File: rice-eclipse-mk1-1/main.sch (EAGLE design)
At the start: 136 parts, among them IC1 LMV321LICTRT, IC2 LMV321LICTRT, IC3 LMV321LICTRT, IC4 LMV321LICTRT, IC5 UA78M, IC6 LMV321LICTRT, IC7 LMV321LICTRT, IC8 LMV321LICTRT, IC9 LMV321LICTRT, U1 LM1084ISX-5.0/NOPB, U2 THS4531IDRD8-M, U3 THS4531IDRD8-M, U4 THS4531IDRD8-M, U5 THS4531IDRD8-M, U6 1101M2S3CQE2

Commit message: Fixed board files maybe.
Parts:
- removed LED4: (no value), led:LED5MM
- added +10V_LED: (no value), led:LED5MM
- added PWR_DEBUG: (no value), con-phoenix-254:MPT5
- added RPI_DEBUG: (no value), con-phoenix-254:MPT7
- C14, C15, C18, C21, C24, C27, C8, C9: value 10nF -> 0.1UF; device rcl:C-USC0402K -> rcl:C-USC0603
- renumbered IC5 to 10V_REG, LED1 to +12V_LED, LED2 to +5V_LED, LED3 to +3.3V_LED, REG1 to 3.3V_REG, U$1 to PWR_IN, U$4 to PWR_OUT1, U$5 to PWR_OUT2, U$6 to SOL+RELAY, U$7 to SOLENOIDS, U1 to 5V_REG
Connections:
- net +10V: now also PWR_DEBUG-2.1, PWR_OUT1G$1.1; no longer PWR_OUT1G$2.2
- net +12V: now also PWR_DEBUG-1.1, PWR_OUT1G$2.2; no longer PWR_OUT1G$1.1
- net +3V3: now also PWR_DEBUG-4.1, PWR_OUT2G$1.1
- net +5V: now also PWR_DEBUG-3.1, PWR_OUT2G$2.2; no longer PWR_OUT2G$1.1
- net ADC1_CS: now also RPI_DEBUG-4.1
- net ADC2_CS: now also RPI_DEBUG-3.1
- net ADC3_CS: now also RPI_DEBUG-2.1
- net GND: now also +10V_LED.C, PWR_DEBUG-5.1, RPI_DEBUG-1.1; no longer LED4.A, PWR_OUT2G$2.2
- net MISO: now also RPI_DEBUG-6.1
- net MOSI: now also RPI_DEBUG-5.1
- net N$9: now also +10V_LED.A; no longer LED4.C
- net SCLK: now also RPI_DEBUG-7.1

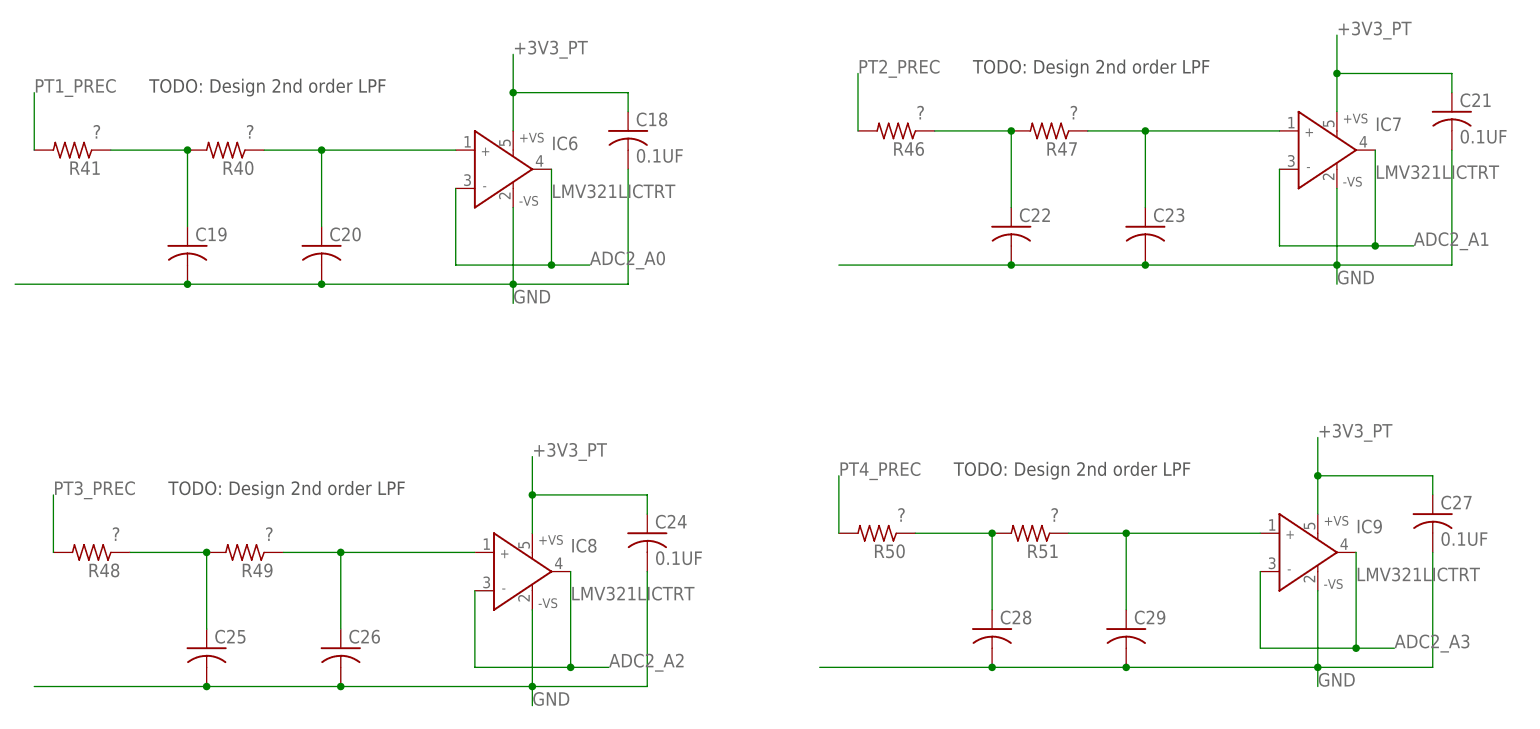
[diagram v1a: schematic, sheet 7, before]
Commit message: Fixed major known bugs in board design.
* 5V power rail for AA voltage follower.
* 10V rail to power PT connector.
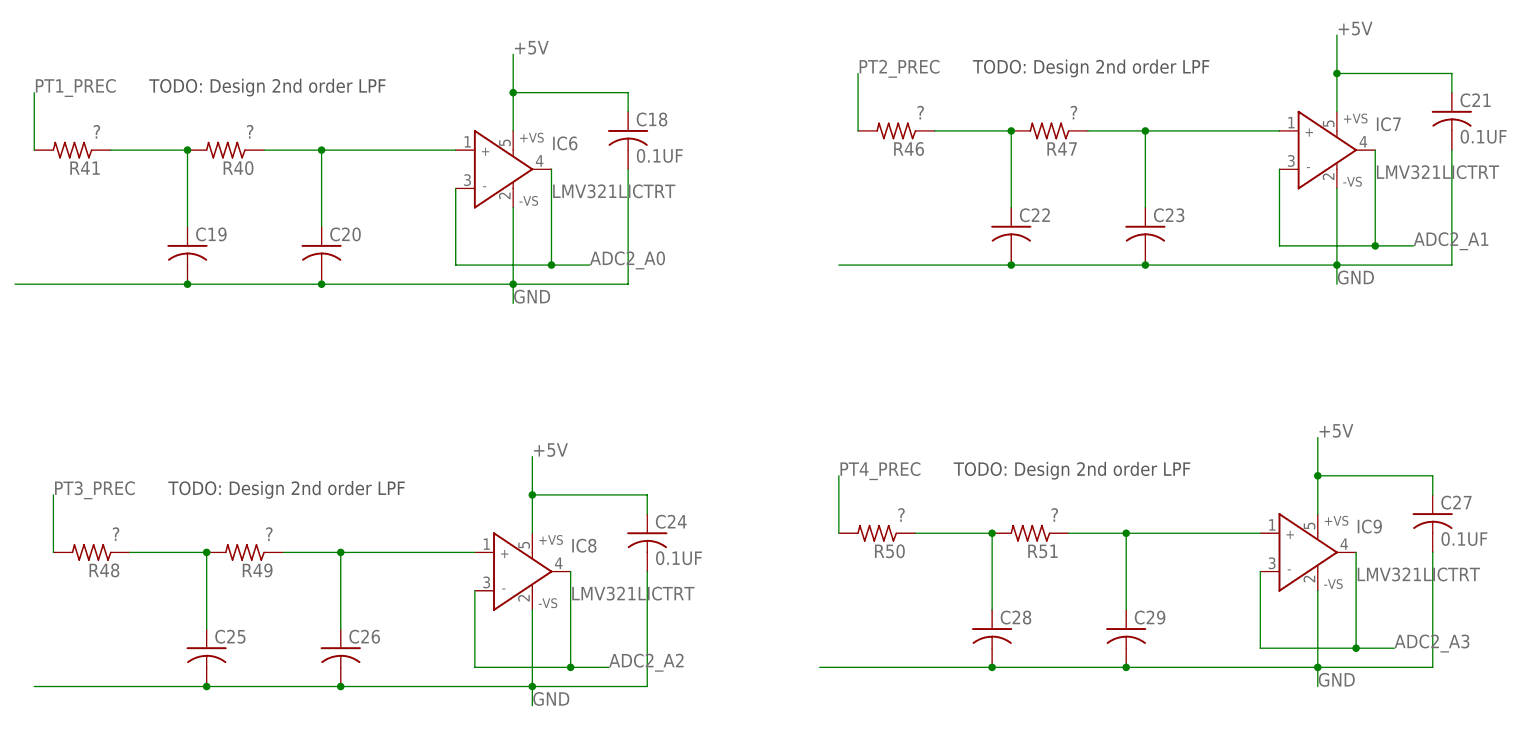
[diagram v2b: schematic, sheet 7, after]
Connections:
- net +10V: now also PT_123_IN-2.SK, PT_123_IN-4.SK, PT_123_IN-6.SK, TC_PT4_IN-6.SK
- net +12V: no longer PT_123_IN-2.SK, PT_123_IN-4.SK, PT_123_IN-6.SK, TC_PT4_IN-6.SK
- net +3V3_PT: no longer C18.1, C21.1, C24.1, C27.1, IC6.+VS, IC7.+VS, IC8.+VS, IC9.+VS
- net +5V: now also C18.1, C21.1, C24.1, C27.1, IC6.+VS, IC7.+VS, IC8.+VS, IC9.+VS
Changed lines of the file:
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@@
 </busses>
 <nets>
-<net name="+3V3_PT" class="0">
-<segment>
-<pinref part="IC6" gate="G$" pin="+VS"/>
-<wire x1="76.2" y1="157.48" x2="76.2" y2="162.56" width="0.1524" layer="91"/>
-<label x="76.2" y="167.64" size="1.778" layer="95"/>
-<pinref part="C18" gate="G$1" pin="1"/>
-<wire x1="76.2" y1="162.56" x2="76.2" y2="167.64" width="0.1524" layer="91"/>
-<wire x1="91.44" y1="160.02" x2="91.44" y2="162.56" width="0.1524" layer="91"/>
-<wire x1="91.44" y1="162.56" x2="76.2" y2="162.56" width="0.1524" layer="91"/>
-<junction x="76.2" y="162.56"/>
-</segment>
-<segment>
-<pinref part="IC7" gate="G$" pin="+VS"/>
-<wire x1="185.42" y1="160.02" x2="185.42" y2="165.1" width="0.1524" layer="91"/>
-<label x="185.42" y="170.18" size="1.778" layer="95"/>
-<pinref part="C21" gate="G$1" pin="1"/>
-<wire x1="185.42" y1="165.1" x2="185.42" y2="170.18" width="0.1524" layer="91"/>
-<wire x1="200.66" y1="162.56" x2="200.66" y2="165.1" width="0.1524" layer="91"/>
-<wire x1="200.66" y1="165.1" x2="185.42" y2="165.1" width="0.1524" layer="91"/>
-<junction x="185.42" y="165.1"/>
-</segment>
-<segment>
-<pinref part="IC8" gate="G$" pin="+VS"/>
-<wire x1="78.74" y1="104.14" x2="78.74" y2="109.22" width="0.1524" layer="91"/>
-<label x="78.74" y="114.3" size="1.778" layer="95"/>
-<pinref part="C24" gate="G$1" pin="1"/>
-<wire x1="78.74" y1="109.22" x2="78.74" y2="114.3" width="0.1524" layer="91"/>
-<wire x1="93.98" y1="106.68" x2="93.98" y2="109.22" width="0.1524" layer="91"/>
-<wire x1="93.98" y1="109.22" x2="78.74" y2="109.22" width="0.1524" layer="91"/>
-<junction x="78.74" y="109.22"/>
-</segment>
-<segment>
-<pinref part="IC9" gate="G$" pin="+VS"/>
-<wire x1="182.88" y1="106.68" x2="182.88" y2="111.76" width="0.1524" layer="91"/>
-<label x="182.88" y="116.84" size="1.778" layer="95"/>
-<pinref part="C27" gate="G$1" pin="1"/>
-<wire x1="182.88" y1="111.76" x2="182.88" y2="116.84" width="0.1524" layer="91"/>
-<wire x1="198.12" y1="109.22" x2="198.12" y2="111.76" width="0.1524" layer="91"/>
-<wire x1="198.12" y1="111.76" x2="182.88" y2="111.76" width="0.1524" layer="91"/>
-<junction x="182.88" y="111.76"/>
-</segment>
-</net>
 <net name="GND" class="0">
 <segment>
@@
 <wire x1="119.38" y1="111.76" x2="119.38" y2="104.14" width="0.1524" layer="91"/>
 <label x="119.38" y="111.76" size="1.778" layer="95"/>
+</segment>
+</net>
+<net name="+5V" class="0">
+<segment>
+<pinref part="IC6" gate="G$" pin="+VS"/>
+<wire x1="76.2" y1="157.48" x2="76.2" y2="162.56" width="0.1524" layer="91"/>
+<label x="76.2" y="167.64" size="1.778" layer="95"/>
+<pinref part="C18" gate="G$1" pin="1"/>
+<wire x1="76.2" y1="162.56" x2="76.2" y2="167.64" width="0.1524" layer="91"/>
+<wire x1="91.44" y1="160.02" x2="91.44" y2="162.56" width="0.1524" layer="91"/>
+<wire x1="91.44" y1="162.56" x2="76.2" y2="162.56" width="0.1524" layer="91"/>
+<junction x="76.2" y="162.56"/>
+</segment>
+<segment>
+<pinref part="IC7" gate="G$" pin="+VS"/>
+<wire x1="185.42" y1="160.02" x2="185.42" y2="165.1" width="0.1524" layer="91"/>
+<label x="185.42" y="170.18" size="1.778" layer="95"/>
+<pinref part="C21" gate="G$1" pin="1"/>
+<wire x1="185.42" y1="165.1" x2="185.42" y2="170.18" width="0.1524" layer="91"/>
+<wire x1="200.66" y1="162.56" x2="200.66" y2="165.1" width="0.1524" layer="91"/>
+<wire x1="200.66" y1="165.1" x2="185.42" y2="165.1" width="0.1524" layer="91"/>
+<junction x="185.42" y="165.1"/>
+</segment>
+<segment>
+<pinref part="IC9" gate="G$" pin="+VS"/>
+<wire x1="182.88" y1="106.68" x2="182.88" y2="111.76" width="0.1524" layer="91"/>
+<label x="182.88" y="116.84" size="1.778" layer="95"/>
+<pinref part="C27" gate="G$1" pin="1"/>
+<wire x1="182.88" y1="111.76" x2="182.88" y2="116.84" width="0.1524" layer="91"/>
+<wire x1="198.12" y1="109.22" x2="198.12" y2="111.76" width="0.1524" layer="91"/>
+<wire x1="198.12" y1="111.76" x2="182.88" y2="111.76" width="0.1524" layer="91"/>
+<junction x="182.88" y="111.76"/>
+</segment>
+<segment>
+<pinref part="IC8" gate="G$" pin="+VS"/>
+<wire x1="78.74" y1="104.14" x2="78.74" y2="109.22" width="0.1524" layer="91"/>
+<label x="78.74" y="114.3" size="1.778" layer="95"/>
+<pinref part="C24" gate="G$1" pin="1"/>
+<wire x1="78.74" y1="109.22" x2="78.74" y2="114.3" width="0.1524" layer="91"/>
+<wire x1="93.98" y1="106.68" x2="93.98" y2="109.22" width="0.1524" layer="91"/>
+<wire x1="93.98" y1="109.22" x2="78.74" y2="109.22" width="0.1524" layer="91"/>
+<junction x="78.74" y="109.22"/>
 </segment>
 </net>
@@
 <net name="+12V" class="0">
 <segment>
+<pinref part="PWR_OUT1" gate="G$2" pin="2"/>
+<wire x1="78.74" y1="162.56" x2="86.36" y2="162.56" width="0.1524" layer="91"/>
+<label x="86.36" y="162.56" size="1.778" layer="95"/>
+</segment>
+</net>
+<net name="+10V" class="0">
+<segment>
+<pinref part="PWR_OUT1" gate="G$1" pin="1"/>
+<wire x1="78.74" y1="165.1" x2="86.36" y2="165.1" width="0.1524" layer="91"/>
+<label x="86.36" y="165.1" size="1.778" layer="95"/>
+</segment>
+<segment>
+<pinref part="PT_123_IN" gate="-2" pin="SK"/>
+<wire x1="30.48" y1="116.84" x2="40.64" y2="116.84" width="0.1524" layer="91"/>
+<label x="40.64" y="116.84" size="1.778" layer="95"/>
+</segment>
+<segment>
+<pinref part="PT_123_IN" gate="-4" pin="SK"/>
+<wire x1="30.48" y1="106.68" x2="40.64" y2="106.68" width="0.1524" layer="91"/>
+<label x="40.64" y="106.68" size="1.778" layer="95"/>
+</segment>
+<segment>
 <pinref part="PT_123_IN" gate="-6" pin="SK"/>
 <wire x1="30.48" y1="96.52" x2="40.64" y2="96.52" width="0.1524" layer="91"/>
@@
 </segment>
 <segment>
-<pinref part="PT_123_IN" gate="-2" pin="SK"/>
-<wire x1="30.48" y1="116.84" x2="40.64" y2="116.84" width="0.1524" layer="91"/>
-<label x="40.64" y="116.84" size="1.778" layer="95"/>
-</segment>
-<segment>
-<pinref part="PT_123_IN" gate="-4" pin="SK"/>
-<wire x1="30.48" y1="106.68" x2="40.64" y2="106.68" width="0.1524" layer="91"/>
-<label x="40.64" y="106.68" size="1.778" layer="95"/>
-</segment>
-<segment>
 <pinref part="TC_PT4_IN" gate="-6" pin="SK"/>
 <wire x1="30.48" y1="66.04" x2="40.64" y2="66.04" width="0.1524" layer="91"/>
 <label x="40.64" y="66.04" size="1.778" layer="95"/>
 </segment>
-<segment>
-<pinref part="PWR_OUT1" gate="G$2" pin="2"/>
-<wire x1="78.74" y1="162.56" x2="86.36" y2="162.56" width="0.1524" layer="91"/>
-<label x="86.36" y="162.56" size="1.778" layer="95"/>
-</segment>
-</net>
-<net name="+10V" class="0">
-<segment>
-<pinref part="PWR_OUT1" gate="G$1" pin="1"/>
-<wire x1="78.74" y1="165.1" x2="86.36" y2="165.1" width="0.1524" layer="91"/>
-<label x="86.36" y="165.1" size="1.778" layer="95"/>
-</segment>
-</net>
+</net>

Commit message: Added our library to Eagle. Updated the LC circuit.
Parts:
- removed C10, C11: 1UF, rcl:C-USC0603
- removed JP3: (no value), pinhead:PINHD-1X2
- removed LC_IN1, LC_IN2: (no value), con-phoenix-250-extra:1770908
- removed R10, R13, R18, R22: (no value), pot-extra:PTD902
- removed R11, R14, R15, R16, R19, R20, R23, R24: 20K, rcl:R-US_R0603
- removed R12, R17, R21, R9: 33K, rcl:R-US_R0603
- removed U2, U3, U4, U5: THS4531IDRD8-M, texas-extra:THS4531IDRD8-M
- added C30, C32, C34: 1UF, rcl:C-USC0805
- added C31, C33, C35: 6.8nF, rcl:C-USC0805
- added CAL1: (no value), con-phoenix-254:MPT2
- added IC10, IC11, IC12, IC5: MCP6N11R, microchip-extra:MCP6N11R
- added JP4: (no value), pinhead:PINHD-1X2
- added RF1, RF2, RF3, RF4, RF5: 20K, rcl:R-US_0204/7
- added RG1, RG2, RG3, RG4: 200, rcl:R-US_0204/7
- added RZ1, RZ2, RZ3, RZ4: (no value), pot:TRIM_US-S64W
- added U$1, U$4: 1991118, con-phoenix-500-extra:1991118
- C12: device rcl:C-USC0603 -> rcl:C-USC0805
- C13: value 1UF -> 6.8nF; device rcl:C-USC0603 -> rcl:C-USC0805
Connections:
- removed net N$14: R10/2.A, R11.1, U2.VIN+
- removed net N$15: R12.1, U3.!PD
- removed net N$16: R13/2.A, R15.1, U3.VIN+
- removed net N$17: R10/1.A, R14.1, U2.VIN-
- removed net N$18: R13/1.A, R16.1, U3.VIN-
- removed net N$19: R17.1, U4.!PD
- removed net N$23: R22/2.A, R23.1, U5.VIN+
- new net CAL: IC10.ENCAL, IC11.ENCAL, IC12.ENCAL
- new net N$39: C33.1, IC11.FG, RF3.2, RG3.2
- new net N$40: C31.2, IC5.OUT, RF1.1
- new net N$41: C31.1, IC5.FG, RF1.2, RG1.2
- new net N$42: IC5.REF, RG1.1, RZ1.S
- new net N$43: IC11.REF, RG3.1, RZ3.S
- new net N$45: C35.2, IC12.OUT, RF4.1
- new net N$46: C35.1, IC12.FG, RF4.2, RG4.2
- new net N$47: IC12.REF, RG4.1, RZ4.S
- net +3V3: now also JP4.1; no longer JP3.1
- net +3V3_LC: now also C30.1, C32.1, C34.1, CAL1-1.1, IC10.+V, IC11.+V, IC12.+V, IC5.+V, JP4.2, RZ1.E, RZ2.E, RZ3.E, RZ4.E; no longer C10.1, C11.1, C13.1, JP3.2, R12.2, R17.2, R21.2, R9.2, U2.VS+, U3.VS+, U4.VS+, U5.VS+
- net ADC1_A0: no longer R11.2, U2.VOUT-
- net ADC1_A1: no longer R14.2, U2.VOUT+
- net ADC1_A2: no longer R15.2, U3.VOUT-
- net ADC1_A3: no longer R16.2, U3.VOUT+
- net ADC1_A4: no longer R19.2, U4.VOUT-
- net ADC1_A5: no longer R20.2, U4.VOUT+
- net ADC1_A6: no longer R23.2, U5.VOUT-
- net ADC1_A7: no longer R24.2, U5.VOUT+
- net GND: now also C30.2, C32.2, C34.2, IC10.-V, IC11.-V, IC12.-V, IC5.-V, RF5.2, RZ1.A, RZ2.A, RZ3.A, RZ4.A; no longer C10.2, C11.2, C13.2, U2.VS-, U3.VS-, U4.VS-, U5.VS-
- net LC_1_OUT+: now also IC5.+, U$4G$3.3; no longer LC_IN1-3.SK, R10/2.S
- net LC_1_OUT-: now also IC5.-, U$4G$4.4; no longer LC_IN1-4.SK, R10/1.S
- net LC_2_OUT+: now also IC10.+, U$4G$1.1; no longer LC_IN1-1.SK, R13/2.S
- net LC_2_OUT-: now also IC10.-, U$4G$2.2; no longer LC_IN1-2.SK, R13/1.S
- net LC_3_OUT+: now also IC11.+, U$1G$3.3; no longer LC_IN2-3.SK, R18/2.S
- net LC_3_OUT-: now also IC11.-, U$1G$4.4; no longer LC_IN2-4.SK, R18/1.S
- net LC_4_OUT+: now also IC12.+, U$1G$1.1; no longer LC_IN2-1.SK, R22/2.S
- net LC_4_OUT-: now also IC12.-, U$1G$2.2; no longer LC_IN2-2.SK, R22/1.S
- net N$13: now also CAL1-2.1, IC5.ENCAL, RF5.1; no longer R9.1, U2.!PD
- net N$20: now also C13.2, IC10.OUT, RF2.1; no longer R18/2.A, R19.1, U4.VIN+
- net N$21: now also C13.1, IC10.FG, RF2.2, RG2.2; no longer R18/1.A, R20.1, U4.VIN-
- net N$22: now also IC10.REF, RG2.1, RZ2.S; no longer R21.1, U5.!PD
- net N$24: now also C33.2, IC11.OUT, RF3.1; no longer R22/1.A, R24.1, U5.VIN-

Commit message: Minor improvements to board.
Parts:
- removed RF5: 20K, rcl:R-US_0204/7
- added D6: 1N4004, diode:1N4004
- added R10: 500k, rcl:R-US_R0805
- added R9: 10k, rcl:R-US_R0805
- added RPD1: 20K, rcl:R-US_R0805
- added SOLENOIDS2: 1991095, con-phoenix-500-extra:1991095
- added U$5: IRF740, transistor-power:IRF740
- C1, C14, C15, C18, C2, C21, C24, C27, C3, C8, C9: device rcl:C-USC0603 -> rcl:C-USC0805
- C19, C22, C25, C28: value (none) -> 470nF; device rcl:C-US025-025X050 -> rcl:C-USC0805
- C20, C23, C26, C29: value (none) -> 4.7nF; device rcl:C-US025-025X050 -> rcl:C-USC0805
- CAL1: device con-phoenix-254:MPT2 -> pinhead:PINHD-1X2
- R1, R2, R25, R29, R3, R30, R4, R5, R6, R7, R8: device rcl:R-US_R0603 -> rcl:R-US_R0805
- R26, R27, R28, R35: device resistor:R-US_R0603 -> resistor:R-US_R0805
- R34, R36, R37, R38, R39, R42, R43, R44, R45, R46, R47, R48, R49, R50, R51, R52, R53, R54, R56, R57, R58, R59, RF1, RF2, RF3, RF4, RG1, RG2, RG3, RG4: device rcl:R-US_0204/7 -> rcl:R-US_R0805
- R40: value ? -> 150K; device rcl:R-US_0204/7 -> rcl:R-US_R0805
- R41: value ? -> 1.5K; device rcl:R-US_0204/7 -> rcl:R-US_R0805
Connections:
- new net CTRL_SOLENOID_4: R9.1
- new net N$14: R10.1, R9.2, U$5.G
- new net N$15: SOLENOIDS2G$2.2
- new net SOLENOID_4_NEGATIVE: D6.A, SOLENOIDS2G$1.1, U$5.D
- net +12V: now also D6.C
- net +3V3_LC: now also CAL1.1; no longer CAL1-1.1
- net GND: now also R10.2, RPD1.2, U$5.S; no longer RF5.2
- net N$13: now also CAL1.2, RPD1.1; no longer CAL1-2.1, RF5.1
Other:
- note added: "NC"

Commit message: Moved onto board. Preliminary power routing.
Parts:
- removed PT_123_IN, TC_PT4_IN: (no value), con-phoenix-250-extra:1770924
- removed U$1, U$4: 1991118, con-phoenix-500-extra:1991118
- added LC1/2, LC3/4, PT1/2, PT3/4, THERMOCOUPLES: 1991118, con-phoenix-500-extra:1991118
- C19, C22, C25, C28: value 470nF -> 68nF
- C20, C23, C26, C29: value 4.7nF -> 680pF
- R31, R32, R33, R55: value 10 -> 22; device rcl:R-US_R0603 -> rcl:R-US_R0805
- R34, R36, R38, R42, R44, R53, R56, R58: value ? -> 20K
- R37, R43, R47, R49, R51, R52, R57: value ? -> 150K
- R39, R45, R54, R59: value ? -> 3K
- R46, R48, R50: value ? -> 1.5K
- renumbered CAL1 to LC_EN/CAL
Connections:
- removed net N$13: IC5.ENCAL, LC_EN/CAL.2, RPD1.1
- removed net N$20: C13.2, IC10.OUT, RF2.1
- removed net N$24: C33.2, IC11.OUT, RF3.1
- removed net N$40: C31.2, IC5.OUT, RF1.1
- removed net N$45: C35.2, IC12.OUT, RF4.1
- removed net RPI_GPIO_18: RPI_GPIO-18.KL
- net +10V: now also PT1/2CON.1, PT1/2G$3.3, PT3/4CON.1, PT3/4G$3.3, PWR_OUT1CON.1; no longer PT_123_IN-2.SK, PT_123_IN-4.SK, PT_123_IN-6.SK, PWR_OUT1G$1.1, TC_PT4_IN-6.SK
- net +12V_DEBUG: now also PWR_INCON.1; no longer PWR_ING$1.1
- net +3V3: now also PWR_OUT2CON.1; no longer PWR_OUT2G$1.1
- net ADC1_A0: now also C31.2, IC5.OUT, RF1.1
- net ADC1_A1: now also C13.2, IC10.OUT, RF2.1
- net ADC1_A2: now also C33.2, IC11.OUT, RF3.1
- net ADC1_A3: now also C35.2, IC12.OUT, RF4.1
- net ADC2_A4: now also THERMOCOUPLESCON.1; no longer TC_PT4_IN-4.SK
- net ADC2_A5: now also THERMOCOUPLESG$2.2; no longer TC_PT4_IN-3.SK
- net ADC2_A6: now also THERMOCOUPLESG$3.3; no longer TC_PT4_IN-2.SK
- net ADC2_A7: now also THERMOCOUPLESG$4.4; no longer TC_PT4_IN-1.SK
- net CAL: now also IC5.ENCAL, LC_EN/CAL.2, RPD1.1
- net CTRL_SOLENOID_4: now also RPI_GPIO-18.KL
- net LC_1_OUT+: now also LC1/2G$3.3; no longer U$4G$3.3
- net LC_1_OUT-: now also LC1/2G$4.4; no longer U$4G$4.4
- net LC_2_OUT+: now also LC1/2CON.1; no longer U$4G$1.1
- net LC_2_OUT-: now also LC1/2G$2.2; no longer U$4G$2.2
- net LC_3_OUT+: now also LC3/4G$3.3; no longer U$1G$3.3
- net LC_3_OUT-: now also LC3/4G$4.4; no longer U$1G$4.4
- net LC_4_OUT+: now also LC3/4CON.1; no longer U$1G$1.1
- net LC_4_OUT-: now also LC3/4G$2.2; no longer U$1G$2.2
- net PT1_VS-: now also PT1/2G$2.2; no longer PT_123_IN-5.SK
- net PT2_VS-: now also PT1/2G$4.4; no longer PT_123_IN-3.SK
- net PT3_VS-: now also PT3/4G$2.2; no longer PT_123_IN-1.SK
- net PT4_VS-: now also PT3/4G$4.4; no longer TC_PT4_IN-5.SK
- net RELAY_NEGATIVE: now also SOL+RELAYCON.1; no longer SOL+RELAYG$1.1
- net SOLENOID_2_NEGATIVE: now also SOLENOIDSCON.1; no longer SOLENOIDSG$1.1
- net SOLENOID_4_NEGATIVE: now also SOLENOIDS2CON.1; no longer SOLENOIDS2G$1.1
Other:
- moved on the sheet: C12, C30, C32, C34
